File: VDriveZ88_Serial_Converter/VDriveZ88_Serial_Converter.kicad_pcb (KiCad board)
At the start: 2 copper layers, 37 x 31 mm, 12 parts, among them J1 VDrive, J2 Z88, J3 Power, U1 MAX232

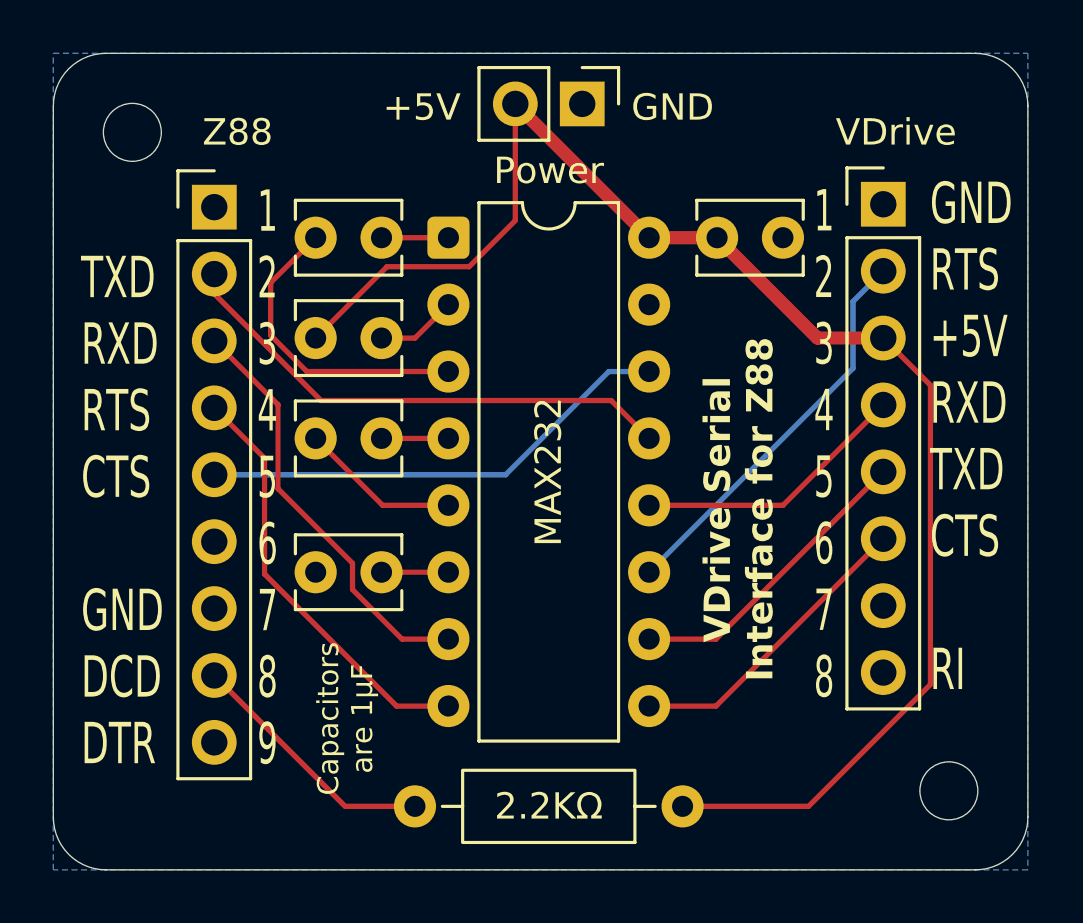
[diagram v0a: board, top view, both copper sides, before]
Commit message: Changed VDrive connector to 2mm pitch
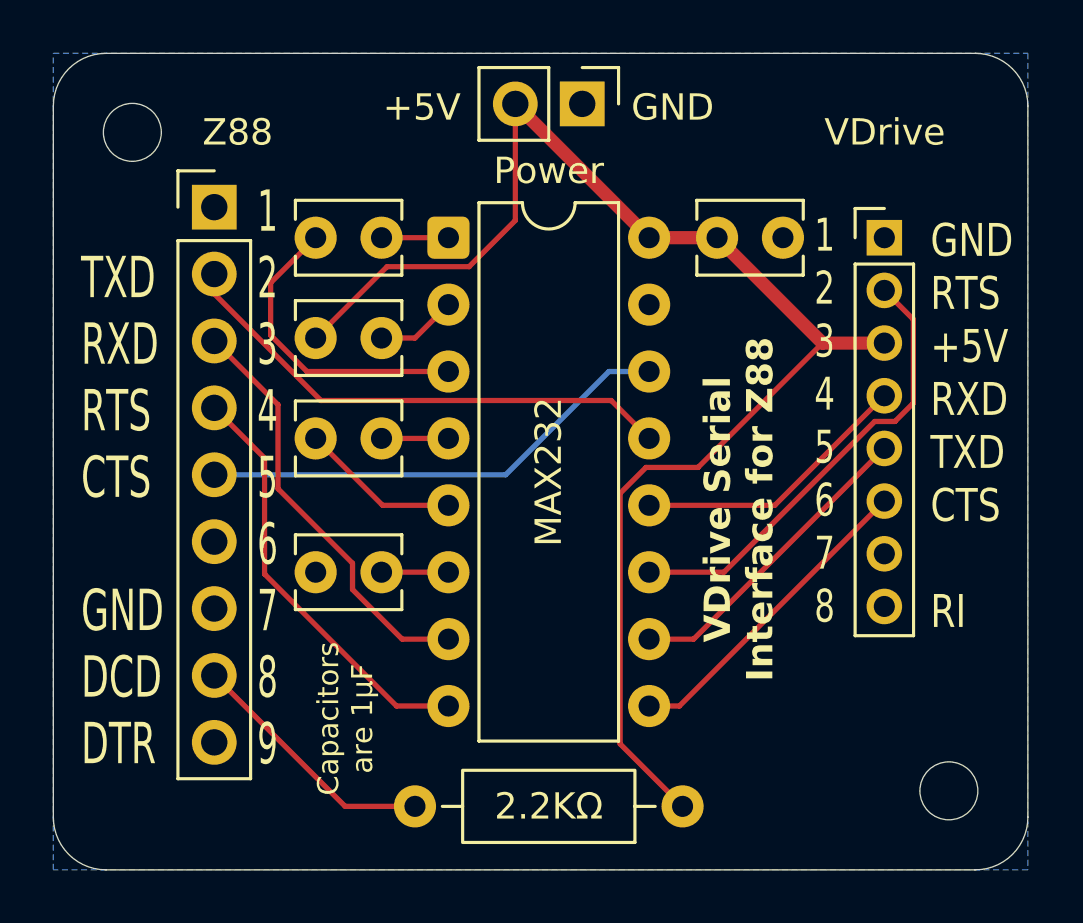
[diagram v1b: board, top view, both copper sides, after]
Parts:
- J1: footprint Connector_PinHeader_2.54mm:PinHeader_1x08_P2.54mm_Vertical -> Connector_PinHeader_2.00mm:PinHeader_1x08_P2.00mm_Vertical
- moved J1 1.27 mm to (98.6, 55.3)
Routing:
- net VD_RTS: track 15.1 -> 17.4 mm
- net +5V: track 56.7 -> 54.5 mm
- net VD_CTS: track 11.5 -> 12.2 mm
